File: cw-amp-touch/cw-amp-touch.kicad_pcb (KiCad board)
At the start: 2 copper layers, 83 x 41 mm, 11 parts, among them J1 Conn_02x05_Odd_Even

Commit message: tidy up folder structure
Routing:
- net +3V3: track 194.2 -> 192.3 mm
- net LED-ANALOG-INT: track 157.4 -> 158.5 mm
- net LED-ANALOG-EXT: track 136.0 -> 136.5 mm

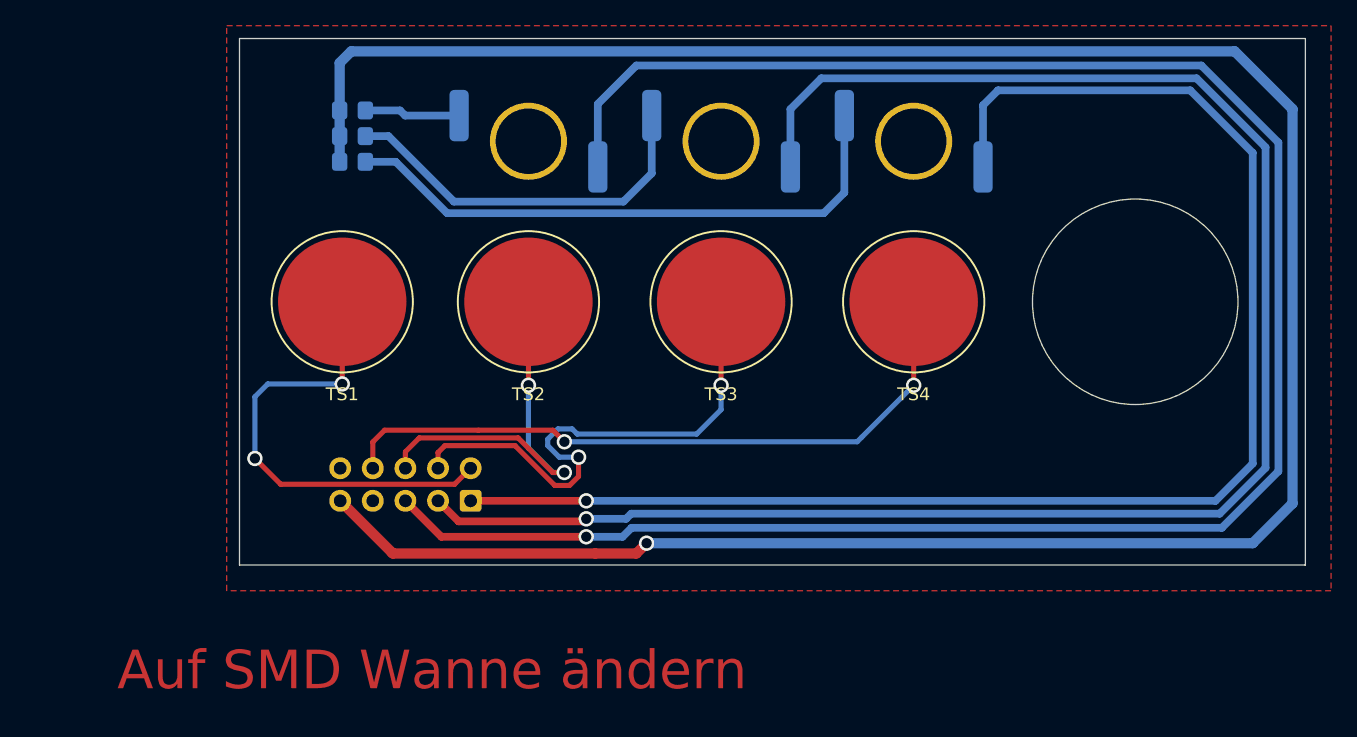
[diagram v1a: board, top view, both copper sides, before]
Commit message: office amp touch: replaced IDC through hole with SMD pinheader
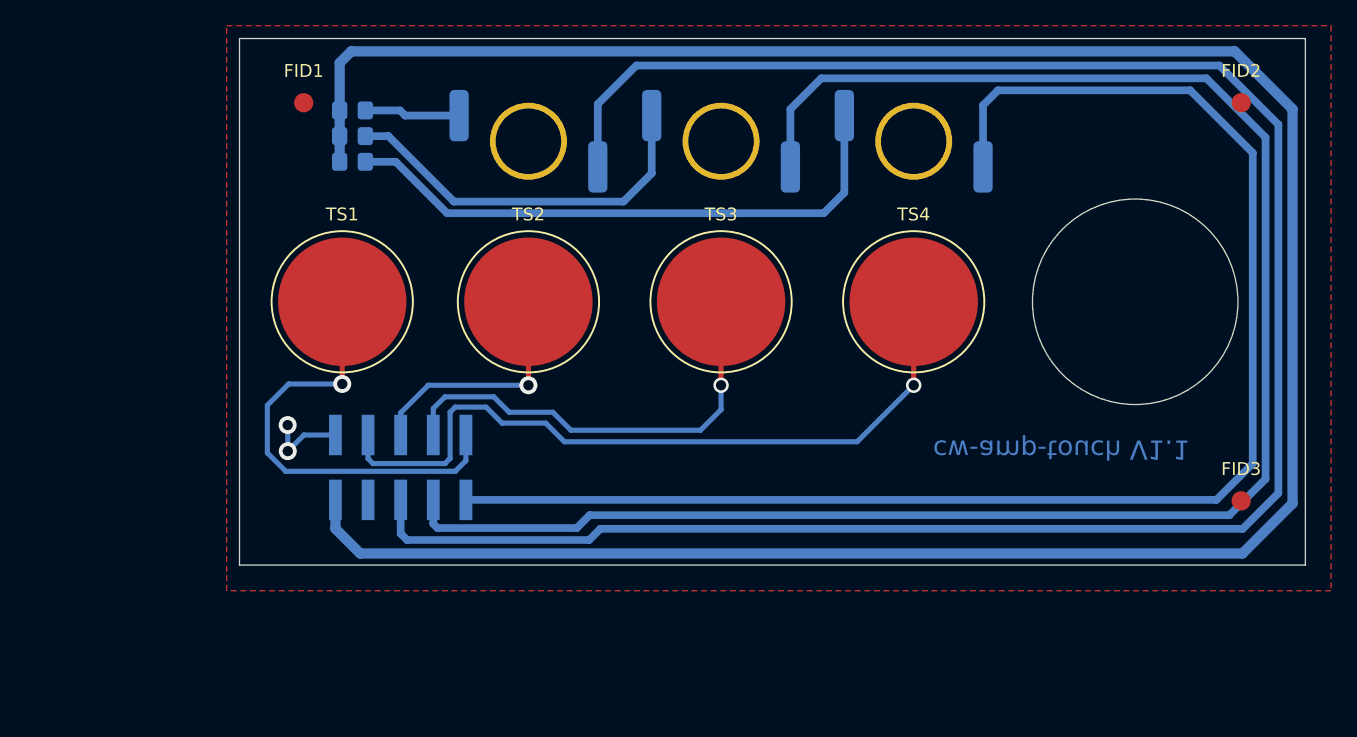
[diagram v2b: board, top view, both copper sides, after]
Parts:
- added FID1: Fiducial, Fiducial:Fiducial_1.5mm_Mask3mm, F.Cu at (135.0, 85.0)
- added FID2: Fiducial, Fiducial:Fiducial_1.5mm_Mask3mm, F.Cu at (208.0, 85.0)
- added FID3: Fiducial, Fiducial:Fiducial_1.5mm_Mask3mm, F.Cu at (208.0, 116.0)
- J1: footprint Connector_IDC:IDC-Header_2x05_P2.54mm_Vertical -> Connector_PinHeader_2.54mm:PinHeader_2x05_P2.54mm_Vertical_SMD
- moved J1 6.04 mm to (142.6, 113.4)
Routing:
- net TOUCH-KEY-ANALOG-INT: track 30.2 -> 19.1 mm, vias 2 -> 1
- net TOUCH-KEY-ANALOG-EXT: track 41.9 -> 35.0 mm, vias 2 -> 1
- net GNDD: track 0.00 -> 6.26 mm, vias 0 -> 2
- net TOUCH-KEY-BT: track 53.2 -> 57.9 mm, vias 2 -> 1
- net LED-ANALOG-INT: track 158.5 -> 162.4 mm, vias 1 -> 0
- net LED-ANALOG-EXT: track 136.5 -> 139.4 mm, vias 1 -> 0
- net +3V3: track 192.3 -> 194.0 mm, vias 1 -> 0
- net TOUCH-KEY-POWER: track 36.6 -> 35.0 mm, vias 2 -> 1
- net LED-BT: track 114.6 -> 114.9 mm, vias 1 -> 0
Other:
- board text added: "cw-amp-touch V1.1"
- board text removed: "Auf SMD Wanne ändern"
